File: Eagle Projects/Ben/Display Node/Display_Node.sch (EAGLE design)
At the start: 41 parts, among them Q1 16MHz, Q3 16MHz, Q4 16MHz, Q5 16MHz, Q6 2N7002, Q7 2N7002, U1 ATMEGA328P_TQFP, U2 MCP2551, X1 5566-6, X2 5566-6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

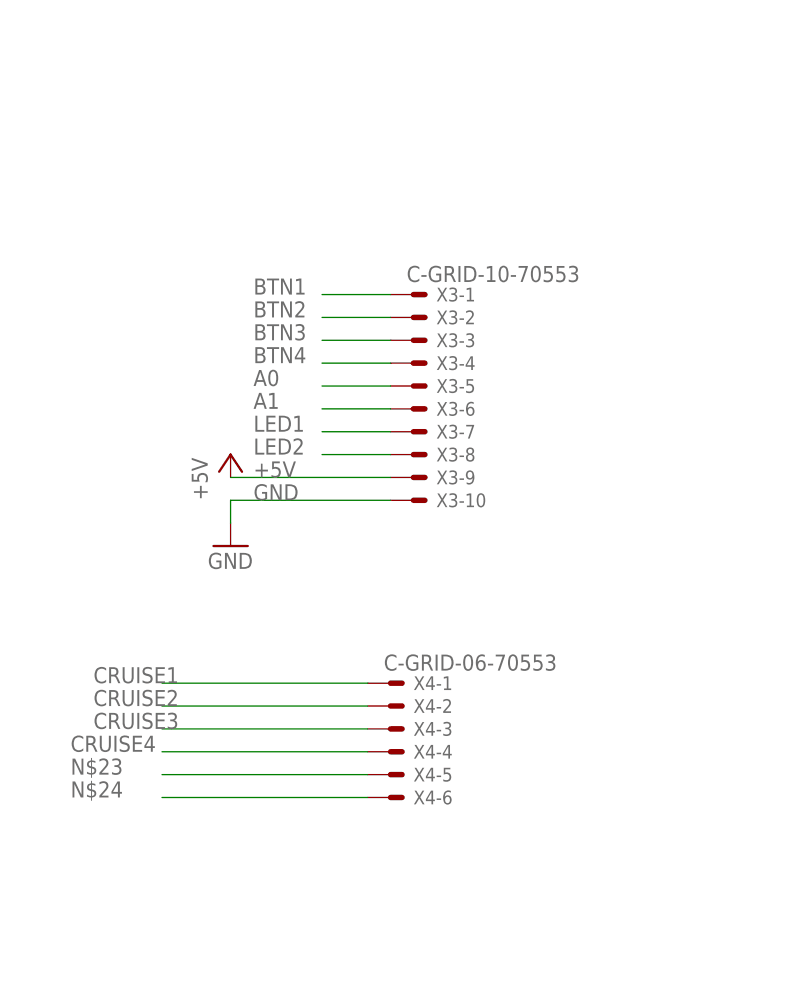
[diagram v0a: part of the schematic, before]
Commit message: Added homebrew TE Connectivity EP 2.5mm TPA Connector series. Only right angle for now..
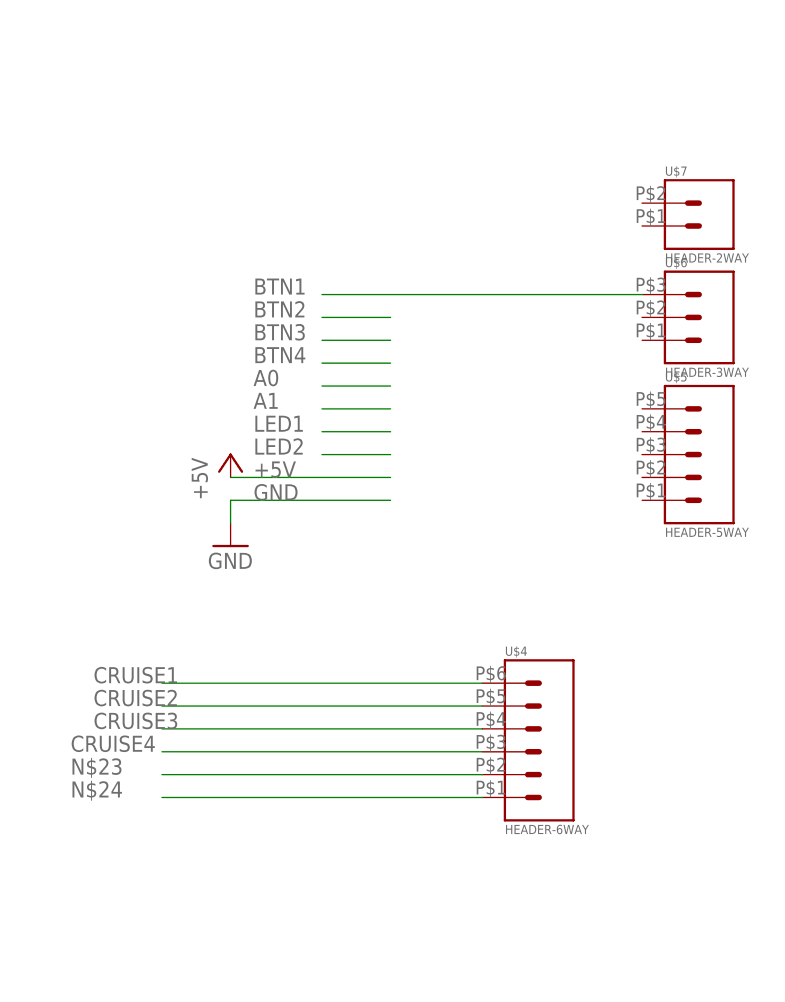
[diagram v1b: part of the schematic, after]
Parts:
- removed X3: C-GRID-10-70553, con-molex:C-GRID-10-70553
- removed X4: C-GRID-06-70553, con-molex:C-GRID-06-70553
- added U$4: HEADER-6WAY, con-TE-EP:HEADER-6WAY
- added U$5: HEADER-5WAY, con-TE-EP:HEADER-5WAY
- added U$6: HEADER-3WAY, con-TE-EP:HEADER-3WAY
- added U$7: HEADER-2WAY, con-TE-EP:HEADER-2WAY
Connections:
- net +5V: no longer X3-9.S
- net A0: no longer X3-5.S
- net A1: no longer X3-6.S
- net BTN1: no longer X3-1.S
- net BTN2: no longer X3-2.S
- net BTN3: no longer X3-3.S
- net BTN4: no longer X3-4.S
- net CRUISE1: now also U$4.P$6; no longer X4-1.S
- net CRUISE2: now also U$4.P$5; no longer X4-2.S
- net CRUISE3: now also U$4.P$4; no longer X4-3.S
- net CRUISE4: now also U$4.P$3; no longer X4-4.S
- net GND: no longer X3-10.S
- net LED1: no longer X3-7.S
- net LED2: no longer X3-8.S
- net N$23: now also U$4.P$2; no longer X4-5.S
- net N$24: now also U$4.P$1; no longer X4-6.S
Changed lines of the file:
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@@
 <part name="R10" library="resistor" deviceset="R-US_" device="R0805" value="1k"/>
 <part name="P+12" library="supply1" deviceset="+5V" device=""/>
-<part name="X4" library="con-molex" deviceset="C-GRID-06" device="-70553"/>
-<part name="X3" library="con-molex" deviceset="C-GRID-10" device="-70553"/>
 <part name="P+13" library="supply1" deviceset="+5V" device=""/>
 <part name="GND14" library="supply1" deviceset="GND" device=""/>
 <part name="S1" library="SparkFun" deviceset="TAC_SWITCH" device="SMD" value="RESET"/>
 <part name="GND15" library="supply1" deviceset="GND" device=""/>
+<part name="U$4" library="con-TE-EP" deviceset="HEADER-6WAY" device=""/>
+<part name="U$5" library="con-TE-EP" deviceset="HEADER-5WAY" device=""/>
+<part name="U$6" library="con-TE-EP" deviceset="HEADER-3WAY" device=""/>
+<part name="U$7" library="con-TE-EP" deviceset="HEADER-2WAY" device=""/>
 </parts>
 <sheets>
@@
 <instance part="R10" gate="G$1" x="38.1" y="91.44" rot="R270"/>
 <instance part="P+12" gate="1" x="33.02" y="101.6"/>
-<instance part="X4" gate="-1" x="195.58" y="22.86"/>
-<instance part="X4" gate="-2" x="195.58" y="20.32"/>
-<instance part="X4" gate="-3" x="195.58" y="17.78"/>
-<instance part="X4" gate="-4" x="195.58" y="15.24"/>
-<instance part="X4" gate="-5" x="195.58" y="12.7"/>
-<instance part="X4" gate="-6" x="195.58" y="10.16"/>
-<instance part="X3" gate="-1" x="198.12" y="66.04"/>
-<instance part="X3" gate="-2" x="198.12" y="63.5"/>
-<instance part="X3" gate="-3" x="198.12" y="60.96"/>
-<instance part="X3" gate="-4" x="198.12" y="58.42"/>
-<instance part="X3" gate="-5" x="198.12" y="55.88"/>
-<instance part="X3" gate="-6" x="198.12" y="53.34"/>
-<instance part="X3" gate="-7" x="198.12" y="50.8"/>
-<instance part="X3" gate="-8" x="198.12" y="48.26"/>
-<instance part="X3" gate="-9" x="198.12" y="45.72"/>
-<instance part="X3" gate="-10" x="198.12" y="43.18"/>
 <instance part="P+13" gate="1" x="177.8" y="48.26"/>
 <instance part="GND14" gate="1" x="177.8" y="38.1"/>
 <instance part="S1" gate="S" x="-48.26" y="106.68" rot="R90"/>
 <instance part="GND15" gate="1" x="-40.64" y="116.84" rot="R90"/>
+<instance part="U$4" gate="G$1" x="210.82" y="17.78"/>
+<instance part="U$5" gate="G$1" x="228.6" y="48.26"/>
+<instance part="U$6" gate="G$1" x="228.6" y="63.5"/>
+<instance part="U$7" gate="G$1" x="228.6" y="76.2"/>
 </instances>
 <busses>
@@
 <segment>
 <label x="180.34" y="43.18" size="1.778" layer="95"/>
-<pinref part="X3" gate="-10" pin="S"/>
 <wire x1="195.58" y1="43.18" x2="177.8" y2="43.18" width="0.1524" layer="91"/>
 <pinref part="GND14" gate="1" pin="GND"/>
@@
 <segment>
 <label x="180.34" y="45.72" size="1.778" layer="95"/>
-<pinref part="X3" gate="-9" pin="S"/>
 <pinref part="P+13" gate="1" pin="+5V"/>
 <wire x1="195.58" y1="45.72" x2="177.8" y2="45.72" width="0.1524" layer="91"/>
@@
 <wire x1="195.58" y1="63.5" x2="187.96" y2="63.5" width="0.1524" layer="91"/>
 <label x="180.34" y="63.5" size="1.778" layer="95"/>
-<pinref part="X3" gate="-2" pin="S"/>
 </segment>
 </net>
@@
 </segment>
 <segment>
-<wire x1="195.58" y1="66.04" x2="187.96" y2="66.04" width="0.1524" layer="91"/>
 <label x="180.34" y="66.04" size="1.778" layer="95"/>
-<pinref part="X3" gate="-1" pin="S"/>
+<wire x1="187.96" y1="66.04" x2="223.52" y2="66.04" width="0.1524" layer="91"/>
 </segment>
 </net>
@@
 <segment>
 <label x="162.56" y="22.86" size="1.778" layer="95"/>
-<pinref part="X4" gate="-1" pin="S"/>
-<wire x1="170.18" y1="22.86" x2="193.04" y2="22.86" width="0.1524" layer="91"/>
+<wire x1="170.18" y1="22.86" x2="205.74" y2="22.86" width="0.1524" layer="91"/>
+<pinref part="U$4" gate="G$1" pin="P$6"/>
 </segment>
 <segment>
@@
 <segment>
 <label x="162.56" y="20.32" size="1.778" layer="95"/>
-<pinref part="X4" gate="-2" pin="S"/>
-<wire x1="170.18" y1="20.32" x2="193.04" y2="20.32" width="0.1524" layer="91"/>
+<wire x1="170.18" y1="20.32" x2="205.74" y2="20.32" width="0.1524" layer="91"/>
+<pinref part="U$4" gate="G$1" pin="P$5"/>
 </segment>
 <segment>
@@
 <segment>
 <label x="162.56" y="17.78" size="1.778" layer="95"/>
-<pinref part="X4" gate="-3" pin="S"/>
-<wire x1="170.18" y1="17.78" x2="193.04" y2="17.78" width="0.1524" layer="91"/>
+<wire x1="170.18" y1="17.78" x2="205.74" y2="17.78" width="0.1524" layer="91"/>
+<pinref part="U$4" gate="G$1" pin="P$4"/>
 </segment>
 <segment>
@@
 <segment>
 <label x="160.02" y="15.24" size="1.778" layer="95"/>
-<pinref part="X4" gate="-4" pin="S"/>
-<wire x1="170.18" y1="15.24" x2="193.04" y2="15.24" width="0.1524" layer="91"/>
+<wire x1="170.18" y1="15.24" x2="205.74" y2="15.24" width="0.1524" layer="91"/>
+<pinref part="U$4" gate="G$1" pin="P$3"/>
 </segment>
 <segment>
@@
 <segment>
 <label x="160.02" y="12.7" size="1.778" layer="95"/>
-<pinref part="X4" gate="-5" pin="S"/>
-<wire x1="170.18" y1="12.7" x2="193.04" y2="12.7" width="0.1524" layer="91"/>
+<wire x1="170.18" y1="12.7" x2="205.74" y2="12.7" width="0.1524" layer="91"/>
+<pinref part="U$4" gate="G$1" pin="P$2"/>
 </segment>
 </net>
@@
 <segment>
 <label x="160.02" y="10.16" size="1.778" layer="95"/>
-<pinref part="X4" gate="-6" pin="S"/>
-<wire x1="170.18" y1="10.16" x2="193.04" y2="10.16" width="0.1524" layer="91"/>
+<wire x1="170.18" y1="10.16" x2="205.74" y2="10.16" width="0.1524" layer="91"/>
+<pinref part="U$4" gate="G$1" pin="P$1"/>
 </segment>
 </net>
@@
 <wire x1="195.58" y1="60.96" x2="187.96" y2="60.96" width="0.1524" layer="91"/>
 <label x="180.34" y="60.96" size="1.778" layer="95"/>
-<pinref part="X3" gate="-3" pin="S"/>
 </segment>
 </net>
@@
 <wire x1="195.58" y1="58.42" x2="187.96" y2="58.42" width="0.1524" layer="91"/>
 <label x="180.34" y="58.42" size="1.778" layer="95"/>
-<pinref part="X3" gate="-4" pin="S"/>
 </segment>
 </net>
@@
 <wire x1="195.58" y1="55.88" x2="187.96" y2="55.88" width="0.1524" layer="91"/>
 <label x="180.34" y="55.88" size="1.778" layer="95"/>
-<pinref part="X3" gate="-5" pin="S"/>
 </segment>
 <segment>
@@
 <wire x1="195.58" y1="53.34" x2="187.96" y2="53.34" width="0.1524" layer="91"/>
 <label x="180.34" y="53.34" size="1.778" layer="95"/>
-<pinref part="X3" gate="-6" pin="S"/>
 </segment>
 <segment>
@@
 <wire x1="195.58" y1="50.8" x2="187.96" y2="50.8" width="0.1524" layer="91"/>
 <label x="180.34" y="50.8" size="1.778" layer="95"/>
-<pinref part="X3" gate="-7" pin="S"/>
 </segment>
 <segment>
@@
 <wire x1="195.58" y1="48.26" x2="187.96" y2="48.26" width="0.1524" layer="91"/>
 <label x="180.34" y="48.26" size="1.778" layer="95"/>
-<pinref part="X3" gate="-8" pin="S"/>
-</segment>
-<segment>
+</segment>
+<segment>

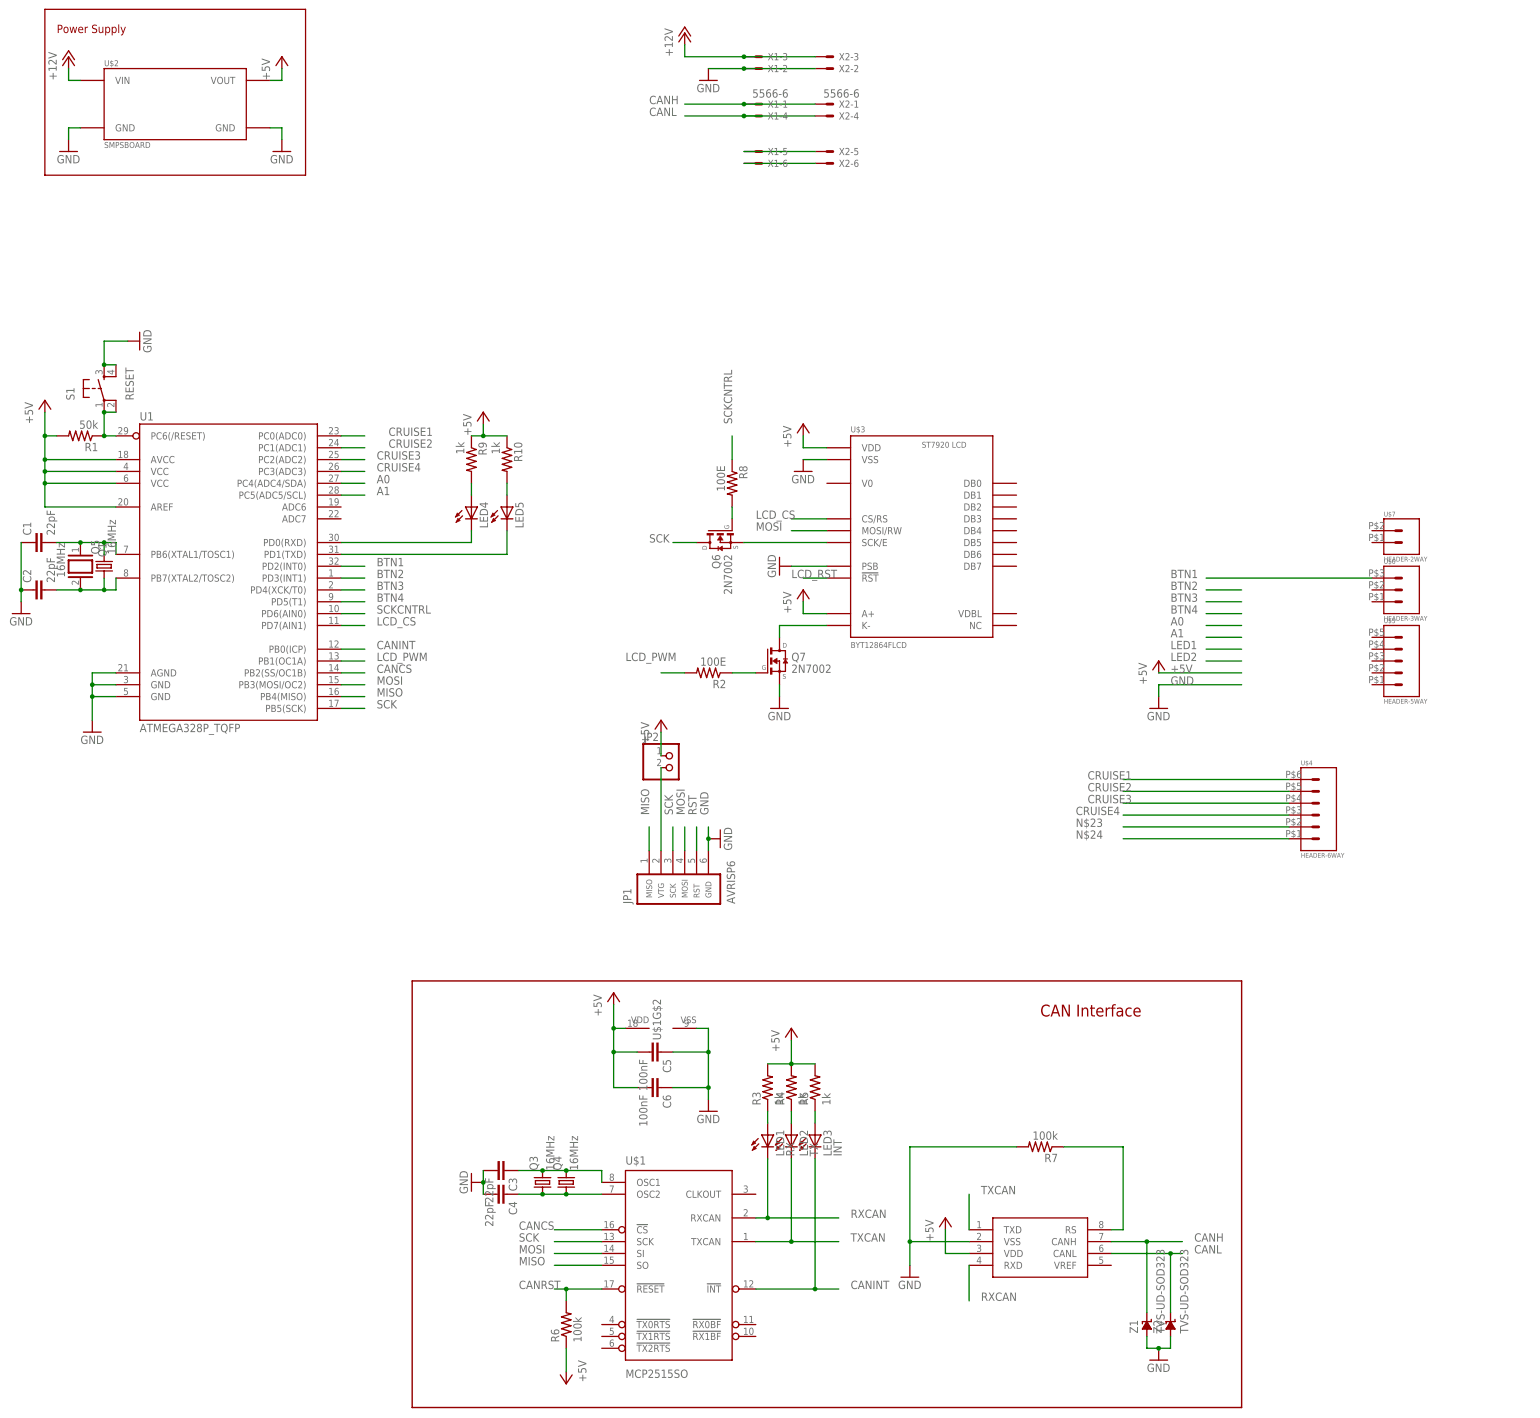
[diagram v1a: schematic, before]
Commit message: Display node nearly done
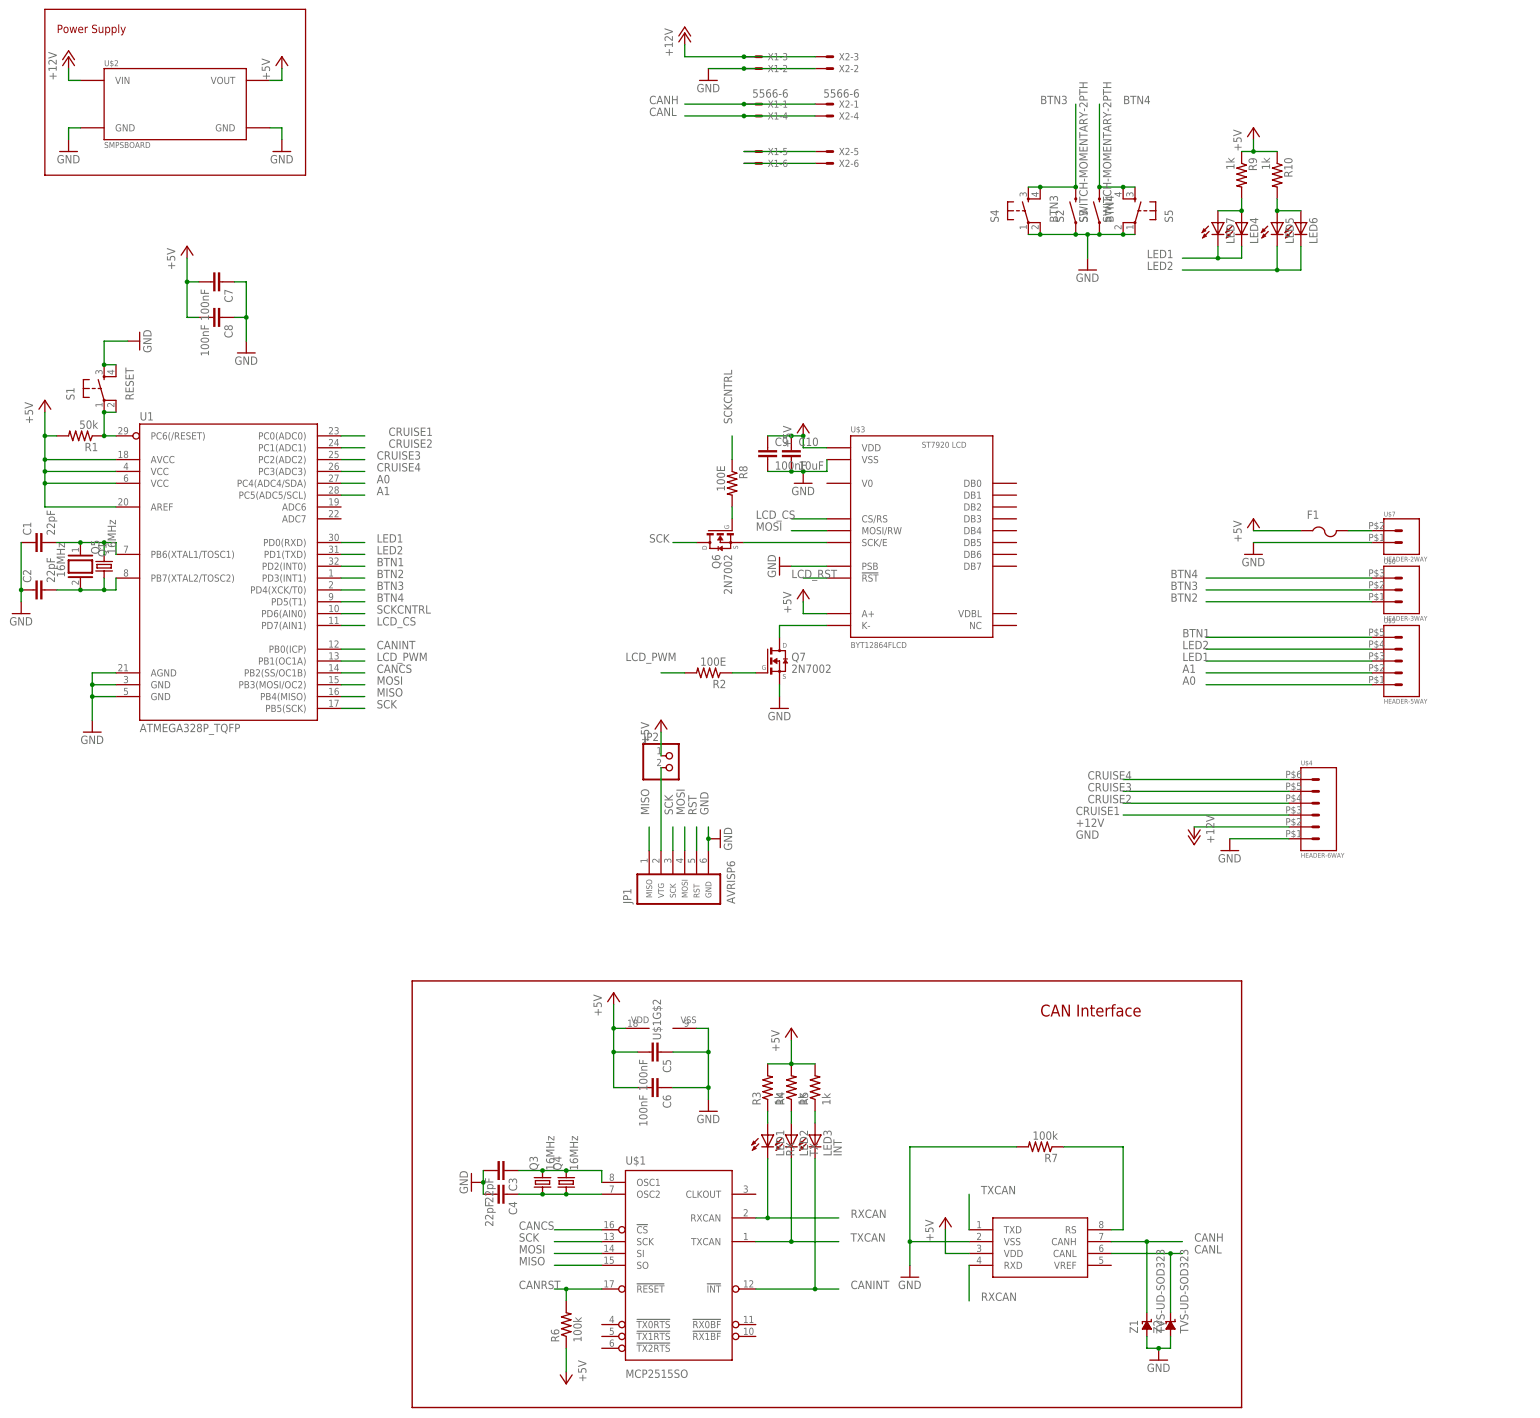
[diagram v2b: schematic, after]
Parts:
- added C10: 10uF, resistor:C-EUC0805
- added C7, C8, C9: 100nF, resistor:C-EUC0805
- added F1: (no value), adafruit:PTCFUSE-1812
- added LED6, LED7: (no value), led:LED5MM
- added S2, S3: SWITCH-MOMENTARY-2PTH, SparkFun:SWITCH-MOMENTARY-2PTH
- added S4: BTN3, SparkFun:TAC_SWITCHSMD
- added S5: BTN4, SparkFun:TAC_SWITCHSMD
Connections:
- removed net N$23: U$4.P$2
- removed net N$24: U$4.P$1
- new net N$17: F1.2, U$7.P$2
- net +12V: now also U$4.P$2
- net +5V: now also C10.1, C7.2, C8.2, C9.1, F1.1
- net A0: now also U$5.P$1
- net A1: now also U$5.P$2
- net BTN1: now also U$5.P$5
- net BTN2: now also U$6.P$1
- net BTN3: now also S2.2, S4.3, S4.4, U$6.P$2
- net BTN4: now also S3.2, S5.3, S5.4, U$6.P$3
- net CRUISE1: now also U$4.P$3; no longer U$4.P$6
- net CRUISE2: now also U$4.P$4; no longer U$4.P$5
- net CRUISE3: now also U$4.P$5; no longer U$4.P$4
- net CRUISE4: now also U$4.P$6; no longer U$4.P$3
- net GND: now also C10.2, C7.1, C8.1, C9.2, S2.1, S3.1, S4.1, S4.2, S5.1, S5.2, U$4.P$1, U$7.P$1
- net LED1: now also LED7.C, U$5.P$3
- net LED2: now also LED6.C, U$5.P$4
- net N$13: now also LED7.A
- net N$16: now also LED6.A
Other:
- moved on the sheet: LED4, LED5, R10, R9

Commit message: Working On Protection
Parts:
- added R11, R12, R13, R14: 470E, resistor:R-US_R0805
- added U$10, U$11, U$8, U$9: DRTR5V0U1SO, RobThePyro:DRTR5V0U1SO
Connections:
- new net N$18: R11.1, U$6.P$3
- new net N$19: R12.1, U$6.P$2
- new net N$20: R13.1, U$6.P$1
- new net N$21: R14.1, U$5.P$5
- net +5V: now also U$10.VCC, U$11.VCC, U$8.VCC, U$9.VCC
- net BTN1: now also R14.2, U$11.I/O; no longer U$5.P$5
- net BTN2: now also R13.2, U$10.I/O; no longer U$6.P$1
- net BTN3: now also R12.2, U$9.I/O; no longer U$6.P$2
- net BTN4: now also R11.2, U$8.I/O; no longer U$6.P$3
- net GND: now also U$10.GND, U$11.GND, U$8.GND, U$9.GND
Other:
- moved on the sheet: F1, U$4, U$5, U$6, U$7
